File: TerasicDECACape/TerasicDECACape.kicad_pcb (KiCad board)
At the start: 4 copper layers, 61.3 x 66.3 mm, 46 parts, among them CN1 NASB0-S6701-TS50, CN2 NASB0-S6701-TS50, J1 MiSTer SDRAM Module, J2 USB_A, J3 Conn_01x03_Male, J4 Conn_02x06_Odd_Even, J5 Conn_02x02_Odd_Even, M1 Sipeed Lichee, P8 BeagleBone_Black_Header, P9 BeagleBone_Black_Header, SW1 TS-1187A-B-A-B, SW2 TS-1187A-B-A-B

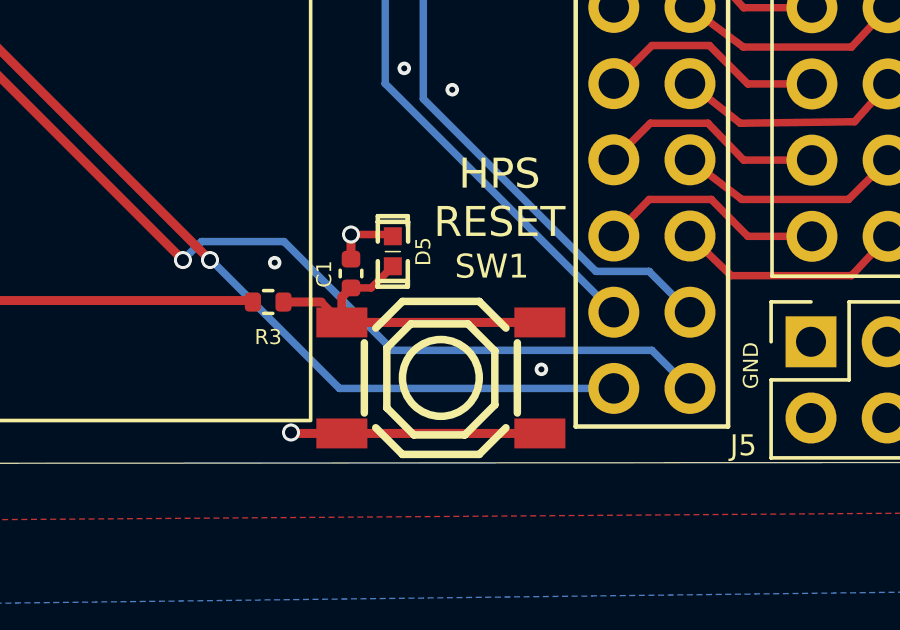
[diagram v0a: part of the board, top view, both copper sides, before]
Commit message: fix tracks running above plane split
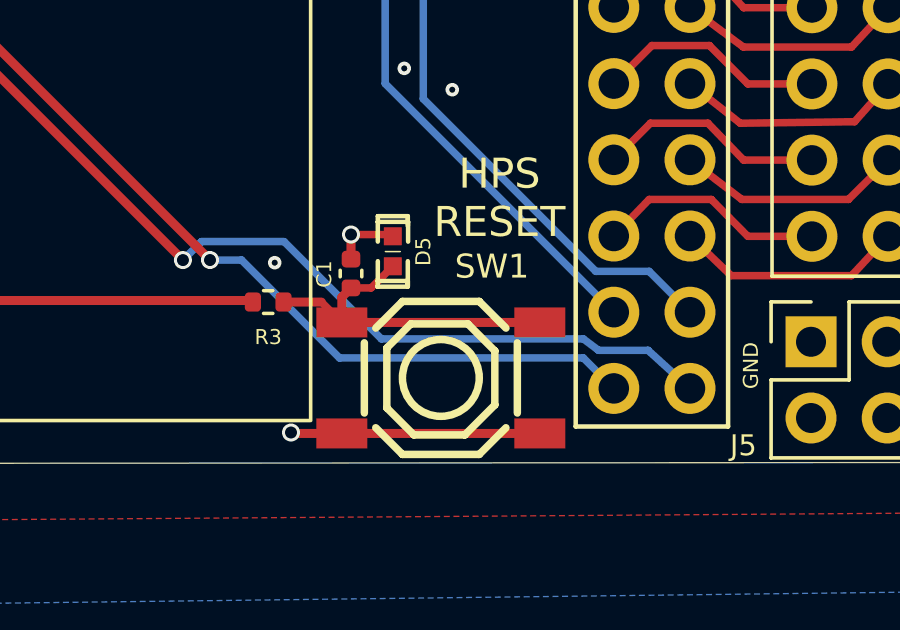
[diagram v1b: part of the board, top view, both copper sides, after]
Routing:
- net GND: vias 155 -> 154
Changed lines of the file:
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@@
   (via (at 146.6701 85.485726) (size 0.45) (drill 0.2) (layers "F.Cu" "B.Cu") (free) (net 1))
   (via (at 124.8791 75.7174) (size 0.45) (drill 0.2) (layers "F.Cu" "B.Cu") (free) (net 1))
-  (via (at 162.2171 117.6274) (size 0.45) (drill 0.2) (layers "F.Cu" "B.Cu") (free) (net 1))
   (via (at 124.0701 104.81365) (size 0.45) (drill 0.2) (layers "F.Cu" "B.Cu") (free) (net 1))
   (via (at 144.7701 74.619066) (size 0.45) (drill 0.2) (layers "F.Cu" "B.Cu") (free) (net 1))
@@
   (segment (start 136.11571 99.8324) (end 150.267905 113.984595) (width 0.3) (layer "F.Cu") (net 155))
   (via (at 150.267905 113.984595) (size 0.6) (drill 0.4) (layers "F.Cu" "B.Cu") (net 155))
-  (segment (start 153.639589 113.367889) (end 157.2641 116.9924) (width 0.25) (layer "B.Cu") (net 155))
+  (segment (start 150.884611 113.367889) (end 153.639589 113.367889) (width 0.25) (layer "B.Cu") (net 155))
+  (segment (start 163.6141 116.6114) (end 164.1221 116.9924) (width 0.25) (layer "B.Cu") (net 155))
+  (segment (start 153.639589 113.367889) (end 156.8831 116.6114) (width 0.25) (layer "B.Cu") (net 155))
   (segment (start 150.267905 113.984595) (end 150.884611 113.367889) (width 0.25) (layer "B.Cu") (net 155))
-  (segment (start 150.884611 113.367889) (end 153.639589 113.367889) (width 0.25) (layer "B.Cu") (net 155))
-  (segment (start 157.2641 116.9924) (end 165.9001 116.9924) (width 0.25) (layer "B.Cu") (net 155))
-  (segment (start 165.9001 116.9924) (end 167.1701 118.2624) (width 0.25) (layer "B.Cu") (net 155))
+  (segment (start 165.7731 116.9924) (end 167.1701 118.2624) (width 0.25) (layer "B.Cu") (net 155))
+  (segment (start 164.1221 116.9924) (end 165.7731 116.9924) (width 0.25) (layer "B.Cu") (net 155))
+  (segment (start 156.8831 116.6114) (end 163.6141 116.6114) (width 0.25) (layer "B.Cu") (net 155))
   (segment (start 136.5201 99.3324) (end 151.1701 113.9824) (width 0.3) (layer "F.Cu") (net 156))
   (segment (start 134.3901 99.3324) (end 136.5201 99.3324) (width 0.3) (layer "F.Cu") (net 156))
   (via (at 151.1701 113.9824) (size 0.6) (drill 0.4) (layers "F.Cu" "B.Cu") (net 156))
-  (segment (start 151.2061 113.9824) (end 155.4861 118.2624) (width 0.25) (layer "B.Cu") (net 156))
-  (segment (start 155.4861 118.2624) (end 164.6301 118.2624) (width 0.25) (layer "B.Cu") (net 156))
-  (segment (start 151.1701 113.9824) (end 151.2061 113.9824) (width 0.25) (layer "B.Cu") (net 156))
+  (segment (start 152.2221 113.9824) (end 155.4861 117.2464) (width 0.25) (layer "B.Cu") (net 156))
+  (segment (start 155.4861 117.2464) (end 163.6141 117.2464) (width 0.25) (layer "B.Cu") (net 156))
+  (segment (start 151.1701 113.9824) (end 152.2221 113.9824) (width 0.25) (layer "B.Cu") (net 156))
+  (segment (start 163.6141 117.2464) (end 164.6301 118.2624) (width 0.25) (layer "B.Cu") (net 156))
   (segment (start 125.7451 91.9324) (end 123.5451 94.1324) (width 0.3) (layer "F.Cu") (net 157))
   (segment (start 123.5451 94.1324) (end 117.6401 94.1324) (width 0.3) (layer "F.Cu") (net 157))

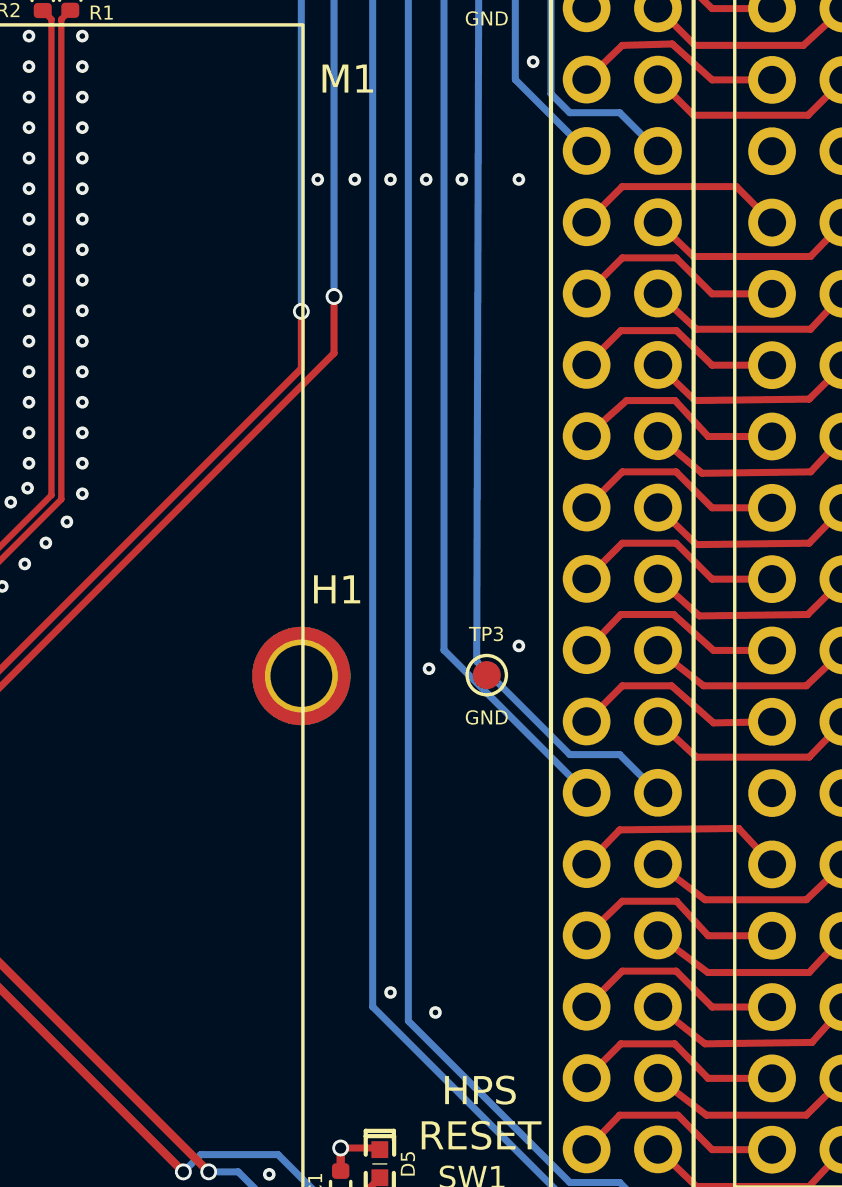
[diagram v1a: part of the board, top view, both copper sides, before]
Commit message: Silkscreen: Add board name, credits and OSHW logo
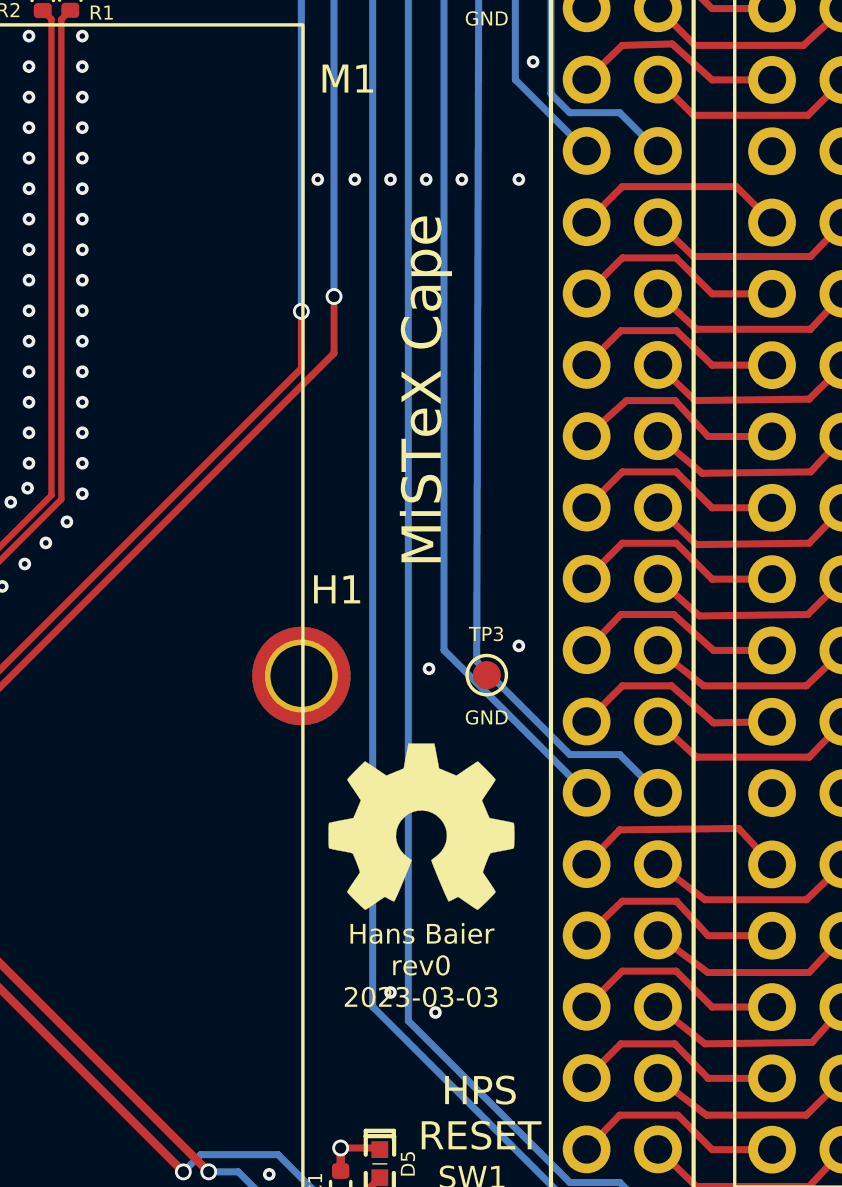
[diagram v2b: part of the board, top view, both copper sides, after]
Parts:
- added N1: OHWLOGO, Symbols:OSHW-Symbol_6.7x6mm_SilkScreen, F.Cu at (158.7, 101.7)
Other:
- board text added: "Hans Baier rev0 2023-03-03"
- board text added: "MiSTeX Cape"
